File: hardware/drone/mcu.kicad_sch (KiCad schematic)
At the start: 18 parts, among them SW1 SW_MEC_5E, U1 STM32N645I0, U6 MX25UW25645GXDI00, Y3 Crystal_GND24

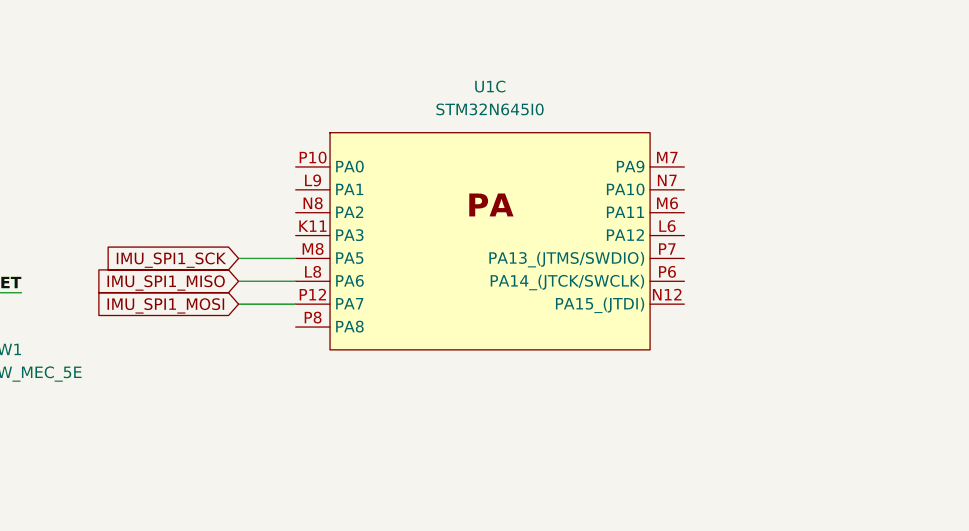
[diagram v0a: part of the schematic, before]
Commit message: Implemented power mux to select between battery and usb c 5V
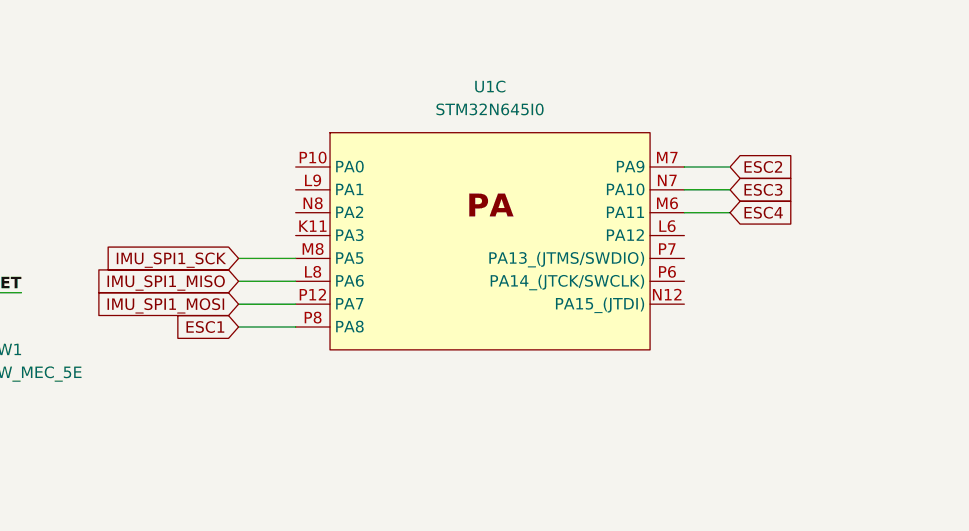
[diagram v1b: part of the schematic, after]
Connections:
- net ESC4: now reaches U1.M6 (PA11)
- net ESC2: now reaches U1.M7 (PA9)
- net ESC3: now reaches U1.N7 (PA10)
- net ESC1: now reaches U1.P8 (PA8)
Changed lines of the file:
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@@
+	(wire
+		(pts
+			(xy 179.07 48.26) (xy 173.99 48.26)
+		)
+		(stroke
+			(width 0)
+			(type default)
+		)
+	)
 	(wire
 		(pts
@@
 	(wire
 		(pts
+			(xy 124.46 60.96) (xy 130.81 60.96)
+		)
+		(stroke
+			(width 0)
+			(type default)
+		)
+	)
+	(wire
+		(pts
 			(xy 82.55 208.28) (xy 102.87 208.28)
 		)
@@
 	(wire
 		(pts
+			(xy 179.07 43.18) (xy 173.99 43.18)
+		)
+		(stroke
+			(width 0)
+			(type default)
+		)
+	)
+	(wire
+		(pts
 			(xy 116.84 191.77) (xy 116.84 187.96)
 		)
@@
 		(pts
 			(xy 143.51 118.11) (xy 137.16 118.11)
+		)
+		(stroke
+			(width 0)
+			(type default)
+		)
+	)
+	(wire
+		(pts
+			(xy 179.07 45.72) (xy 173.99 45.72)
 		)
 		(stroke
@@
 		)
 	)
+	(global_label "ESC1"
+		(shape input)
+		(at 124.46 60.96 180)
+		(fields_autoplaced yes)
+		(effects
+			(font
+				(size 1.27 1.27)
+			)
+			(justify right)
+		)
+		(property "Intersheetrefs" "${INTERSHEET_REFS}"
+			(at 116.6368 60.96 0)
+			(hide yes)
+			(show_name no)
+			(do_not_autoplace no)
+			(effects
+				(font
+					(size 1.27 1.27)
+				)
+				(justify right)
+			)
+		)
+	)
 	(global_label "PWR_ON"
 		(shape input)
@@
 		)
 	)
+	(global_label "ESC2"
+		(shape input)
+		(at 179.07 43.18 0)
+		(fields_autoplaced yes)
+		(effects
+			(font
+				(size 1.27 1.27)
+			)
+			(justify left)
+		)
+		(property "Intersheetrefs" "${INTERSHEET_REFS}"
+			(at 186.8932 43.18 0)
+			(hide yes)
+			(show_name no)
+			(do_not_autoplace no)
+			(effects
+				(font
+					(size 1.27 1.27)
+				)
+				(justify left)
+			)
+		)
+	)
 	(global_label "GNSS_UART4_TX_1V8"
 		(shape input)
@@
 		)
 	)
+	(global_label "ESC3"
+		(shape input)
+		(at 179.07 45.72 0)
+		(fields_autoplaced yes)
+		(effects
+			(font
+				(size 1.27 1.27)
+			)
+			(justify left)
+		)
+		(property "Intersheetrefs" "${INTERSHEET_REFS}"
+			(at 186.8932 45.72 0)
+			(hide yes)
+			(show_name no)
+			(do_not_autoplace no)
+			(effects
+				(font
+					(size 1.27 1.27)
+				)
+				(justify left)
+			)
+		)
+	)
 	(global_label "CC_SDMMC1_D1"
 		(shape input)
@@
 			)
 		)
+	)
+	(global_label "ESC4"
+		(shape input)
+		(at 179.07 48.26 0)
+		(fields_autoplaced yes)
+		(effects
+			(font
+				(size 1.27 1.27)
+			)
+			(justify left)
+		)
+		(property "Intersheetrefs" "${INTERSHEET_REFS}"
+			(at 186.8932 48.26 0)
+			(hide yes)
+			(show_name no)
+			(do_not_autoplace no)
+			(effects
+				(font
+					(size 1.27 1.27)
+				)
+				(justify left)
+			)
+		)

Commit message: Added barometer, more pinmuxxing, added VBAT sensing and reverse voltage protection
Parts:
- added C92: 100n, symbol Device:C
- added R25, R26: 49.9k, BM08BSRSSTBLFSN, symbol Device:R
- added R27: 2.49k, BM08BSRSSTBLFSN, symbol Device:R
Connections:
- net GND: now also C92.2, R27.1
- net at U1.L6 (PA12): now also C92.1, R26.1, R27.2
- net CODEC_I2C2_SCL renamed I2C2_SCL
- net CODEC_I2C2_SDA renamed I2C2_SDA
- new net: R25.1, R26.2
- new net VBAT: R25.2
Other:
- moved on the sheet: R13, R14, U1D, U1F, U1G

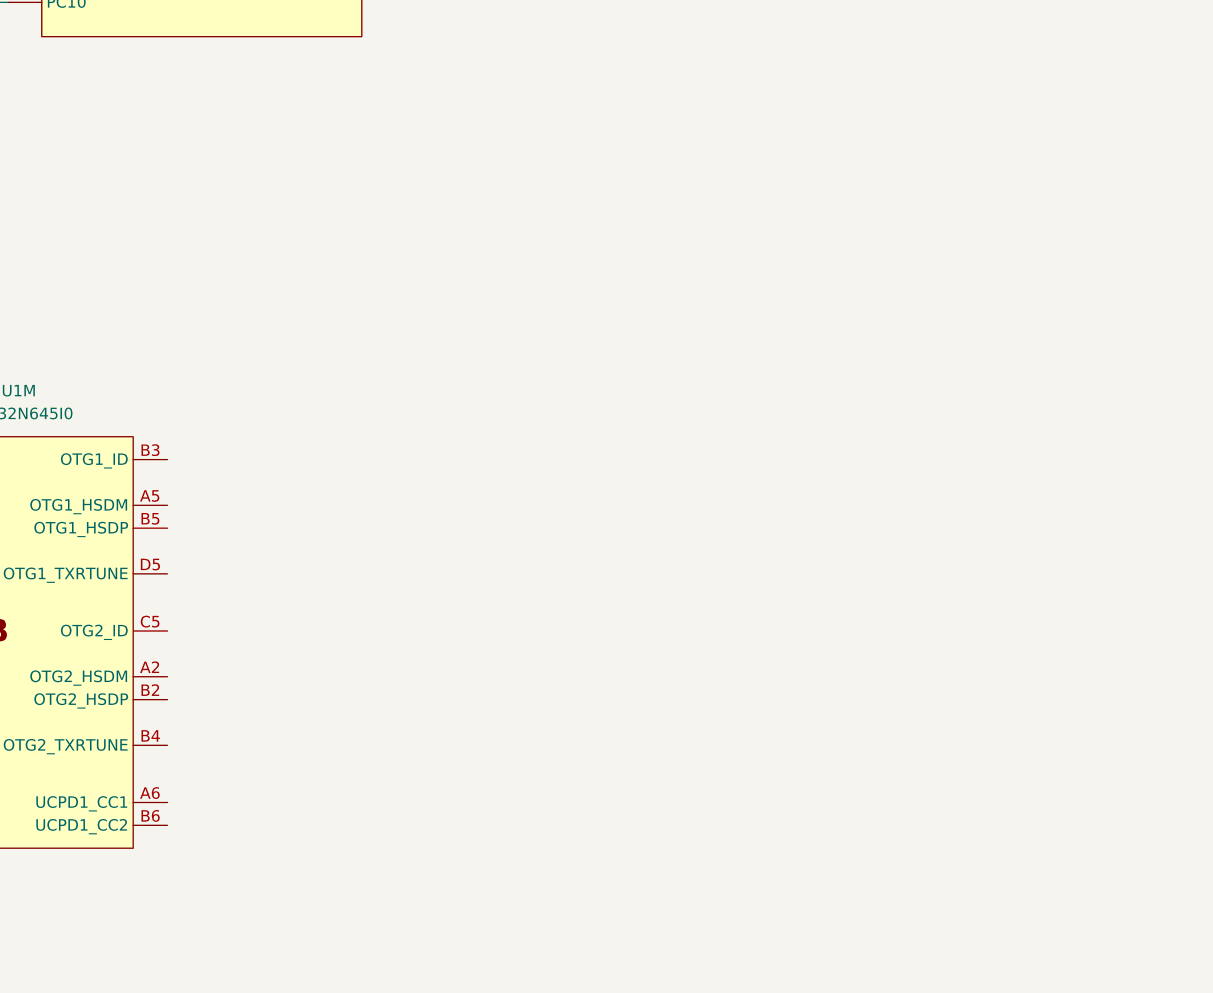
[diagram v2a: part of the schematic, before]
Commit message: Added USB C
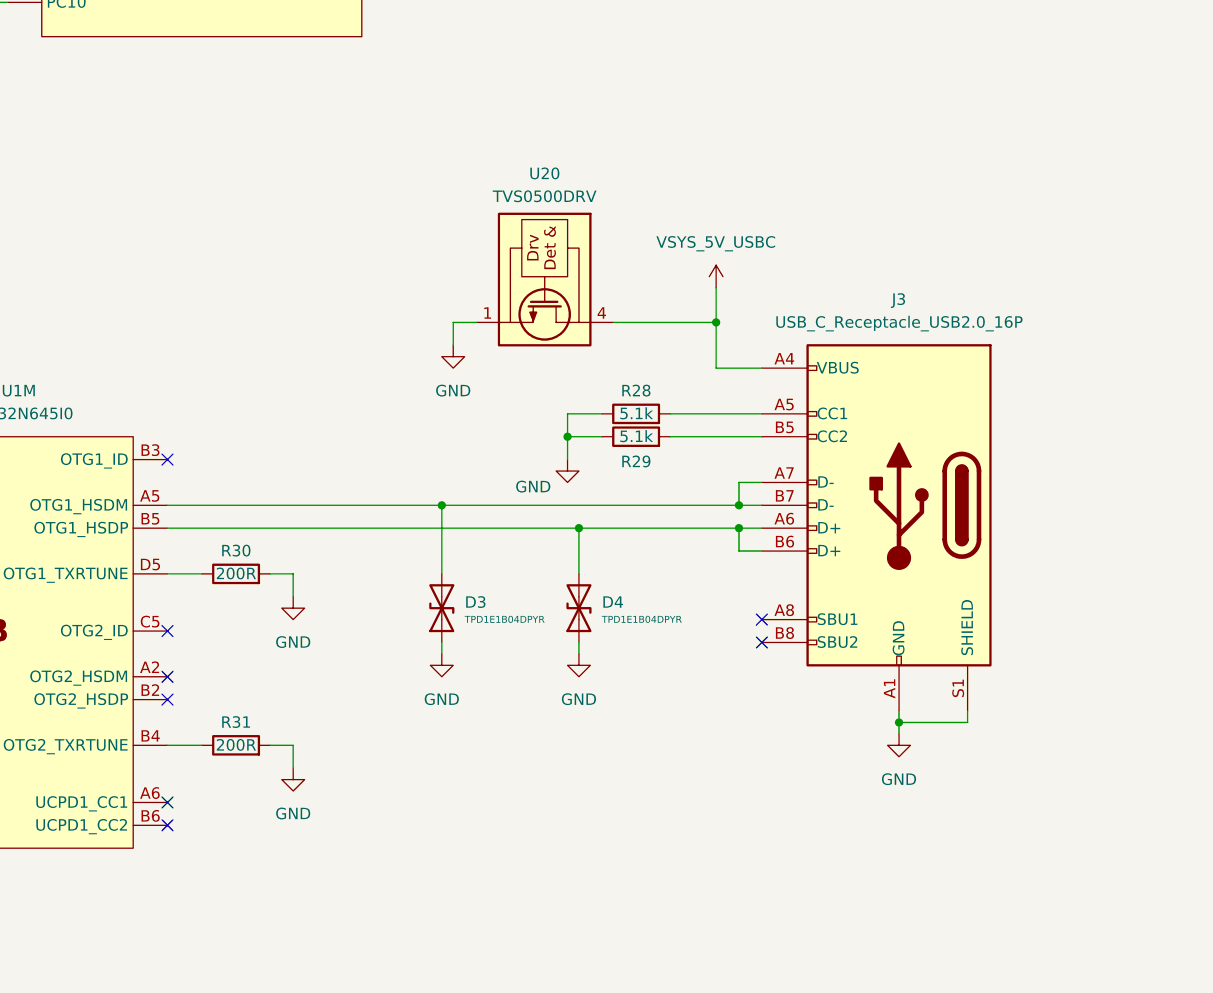
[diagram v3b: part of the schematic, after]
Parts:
- added D3, D4: TPD1E1B04DPYR, Package_DIP:DIP-40_W15.24mm, symbol Device:D_TVS
- added J3: USB_C_Receptacle_USB2.0_16P, symbol Connector:USB_C_Receptacle_USB2.0_16P
- added R28, R29: 5.1k, BM08BSRSSTBLFSN, symbol Device:R
- added R30, R31: 200R, symbol Device:R
- added U20: TVS0500DRV, Package_SON:WSON-6-1EP_2x2mm_P0.65mm_EP1x1.6mm, symbol Power_Protection:TVS0500DRV
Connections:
- net GND: now also D3.1 (A1), D4.1 (A1), J3.A1 (GND), J3.A12 (GND), J3.B1 (GND), J3.B12 (GND), J3.S1 (SHIELD), R28.1, R29.1, R30.2, R31.2, U20.1 (GND), U20.2 (GND), U20.3 (GND), U20.7 (GND)
- net at U1.A5 (OTG1_HSDM): now also D3.2 (A2), J3.A7 (D-), J3.B7 (D-)
- net at U1.B4 (OTG2_TXRTUNE): now also R31.1
- net at U1.B5 (OTG1_HSDP): now also D4.2 (A2), J3.A6 (D+), J3.B6 (D+)
- net at U1.D5 (OTG1_TXRTUNE): now also R30.1
- new net: J3.A5 (CC1), R28.2
- new net: J3.B5 (CC2), R29.2
- new net VSYS_5V_USBC: J3.A4 (VBUS), J3.A9 (VBUS), J3.B4 (VBUS), J3.B9 (VBUS), U20.4 (IN), U20.5 (IN), U20.6 (IN)
- no-connect marks 0 -> 8

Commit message: Added SWD
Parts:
- added C93: 10u, symbol Device:C
- added C94: 100n, symbol Device:C
- added J4: Conn_ARM_SWD_TagConnect_TC2030, Connector:Tag-Connect_TC2030-IDC-FP_2x03_P1.27mm_Vertical, symbol Connector:Conn_ARM_SWD_TagConnect_TC2030
- C1: value C -> 10n
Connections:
- net GND: now also C93.2, C94.2, J4.5 (GND)
- net VDD1V8: now also J4.1 (VCC)
- net VSYS_5V_USBC: now also C93.1, C94.1
- net SWO: now reaches U1.M11 (PB5_(JTDO/TRACESWO))
- net SWO: now also J4.6 (SWO)
- net SWCLK: now reaches U1.P6 (PA14_(JTCK/SWCLK))
- net SWCLK: now also J4.4 (SWCLK)
- net SWDIO: now reaches U1.P7 (PA13_(JTMS/SWDIO))
- net SWDIO: now also J4.2 (SWDIO)
- net RESET renamed NRST
- net NRST: now also J4.3 (~{RESET})
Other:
- note added: "USB C"
- moved on the sheet: C29, C30, C31, C32, C33, C34, D3, D4, J3, R28, R29, R30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

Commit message: Finished MCU schematic decoupling, finished system control schematic
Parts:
- added R32: 10k, symbol Device:R
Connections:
- net GND: now also R32.2
- net VDDA1V8: now also U1.A1 (PDR_ON)
- net at U1.D3 (BOOT0): now also R32.1
- net I2C1_SDA: now reaches U1.B8 (PC1)
- net IMU_CS: now reaches U1.G14 (PB0)
- net IMU_SPI4_MOSI: now reaches U1.H13 (PB7)
- net IMU_SPI4_MISO: now reaches U1.H14 (PB6)
- net IMU_SPI4_SCK: now reaches U1.F14 (PE2)
- net I2C1_SCL: now reaches U1.C8 (PH9)
- net IMU_SPI1_MISO: no longer names the net of U1.L8 (PA6)
- net IMU_SPI1_MOSI: no longer names the net of U1.P12 (PA7)
- net IMU_SPI1_SCK: no longer names the net of U1.M8 (PA5)
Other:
- moved on the sheet: R13, R14, U1G

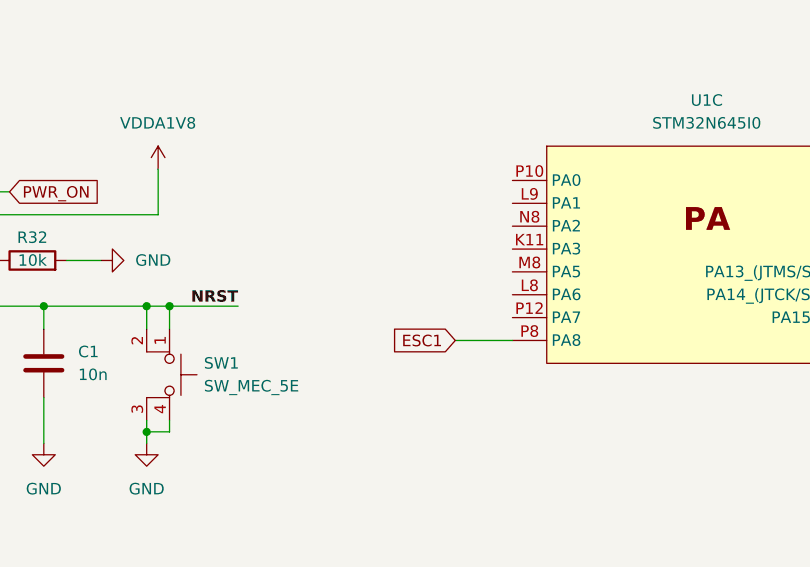
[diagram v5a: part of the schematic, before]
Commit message: Fixed BOOT1 pulldown
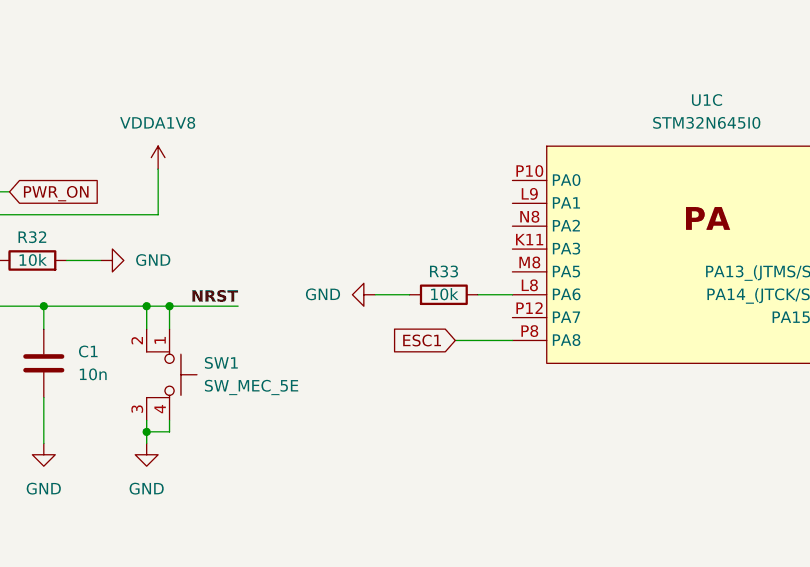
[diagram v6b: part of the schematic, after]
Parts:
- added R33: 10k, symbol Device:R
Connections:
- net GND: now also R33.2
- net at U1.L8 (PA6): now also R33.1
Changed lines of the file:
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@@
+	(wire
+		(pts
+			(xy 130.81 55.88) (xy 127 55.88)
+		)
+		(stroke
+			(width 0)
+			(type default)
+		)
+	)
 	(wire
 		(pts
@@
 		(pts
 			(xy 125.73 170.18) (xy 125.73 171.45)
+		)
+		(stroke
+			(width 0)
+			(type default)
+		)
+	)
+	(wire
+		(pts
+			(xy 119.38 55.88) (xy 115.57 55.88)
 		)
 		(stroke
@@
 					(unit 1)
 				)
+			)
+		)
+	)
+	(symbol
+		(lib_id "Device:R")
+		(at 123.19 55.88 270)
+		(mirror x)
+		(unit 1)
+		(body_style 1)
+		(exclude_from_sim no)
+		(in_bom yes)
+		(on_board yes)
+		(in_pos_files yes)
+		(dnp no)
+		(property "Reference" "R33"
+			(at 123.19 53.34 90)
+			(show_name no)
+			(do_not_autoplace no)
+			(effects
+				(font
+					(size 1.27 1.27)
+				)
+			)
+		)
+		(property "Value" "10k"
+			(at 123.19 55.88 90)
+			(show_name no)
+			(do_not_autoplace no)
+			(effects
+				(font
+					(size 1.27 1.27)
+				)
+			)
+		)
+		(property "Footprint" ""
+			(at 123.19 57.658 90)
+			(hide yes)
+			(show_name no)
+			(do_not_autoplace no)
+			(effects
+				(font
+					(size 1.27 1.27)
+				)
+			)
+		)
+		(property "Datasheet" ""
+			(at 123.19 55.88 0)
+			(hide yes)
+			(show_name no)
+			(do_not_autoplace no)
+			(effects
+				(font
+					(size 1.27 1.27)
+				)
+			)
+		)
+		(property "Description" "Resistor"
+			(at 123.19 55.88 0)
+			(hide yes)
+			(show_name no)
+			(do_not_autoplace no)
+			(effects
+				(font
+					(size 1.27 1.27)
+				)
+			)
+		)
+		(pin "1"
+		)
+		(pin "2"
+		)
+		(instances
+			(project "drone"
+				(path "/62c402a6-ed3f-446b-8423-821e9cc6908b/93cf7a35-4ece-42f4-8b64-ee97cf1aaf17"
+					(reference "R33")
+					(unit 1)
+				)
+			)
+		)
+	)
+	(symbol
+		(lib_id "power:GND")
+		(at 115.57 55.88 270)
+		(mirror x)
+		(unit 1)
+		(body_style 1)
+		(exclude_from_sim no)
+		(in_bom yes)
+		(on_board yes)
+		(in_pos_files yes)
+		(dnp no)
+		(fields_autoplaced yes)
+		(property "Reference" "#PWR0184"
+			(at 109.22 55.88 0)
+			(hide yes)
+			(show_name no)
+			(do_not_autoplace no)
+			(effects
+				(font
+					(size 1.27 1.27)
+				)
+			)
+		)
+		(property "Value" "GND"
+			(at 111.76 55.8799 90)
+			(show_name no)
+			(do_not_autoplace no)
+			(effects
+				(font
+					(size 1.27 1.27)
+				)
+				(justify right)
+			)
+		)
+		(property "Footprint" ""
+			(at 115.57 55.88 0)
+			(hide yes)
+			(show_name no)
+			(do_not_autoplace no)
+			(effects
+				(font
+					(size 1.27 1.27)
+				)
+			)
+		)
+		(property "Datasheet" ""
+			(at 115.57 55.88 0)
+			(hide yes)
+			(show_name no)
+			(do_not_autoplace no)
+			(effects
+				(font
+					(size 1.27 1.27)
+				)
+			)
+		)
+		(property "Description" "Power symbol creates a global label with name \"GND\" , ground"
+			(at 115.57 55.88 0)
+			(hide yes)
+			(show_name no)
+			(do_not_autoplace no)
+			(effects
+				(font
+					(size 1.27 1.27)
+				)
+			)
+		)
+		(pin "1"
+		)
+		(instances
+			(project "drone"
+				(path "/62c402a6-ed3f-446b-8423-821e9cc6908b/93cf7a35-4ece-42f4-8b64-ee97cf1aaf17"
+					(reference "#PWR0184")
+					(unit 1)
+				)

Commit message: Created pinmux table and completed pinmuxing
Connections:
- net CODEC_SAI2_SD_B: no longer U1.J4 (PF5)
- net GNSS_RESET_N_1V8: now reaches U1.A13 (PD3)
- net EN_MODULE: now reaches U1.B11 (PD7)
- net GNSS_TIMEPULSE: now reaches U1.E10 (PD2)
- net CC_IRQ_WL: now reaches U1.A8 (PC6)
- net CC_RESET: now reaches U1.A9 (PC7)
- net IMU_INT1: now reaches U1.M10 (PB12)
- net NRST_CAM: now reaches U1.B10 (PE15)
- net CODEC_IRQ: now reaches U1.C9 (PE14)
- net BARO_IRQ: now reaches U1.L12 (PG8)
- net SX_IRQ: now reaches U1.J3 (PF10)
- net SX_NRST: now reaches U1.L1 (PF8)
- net SX_BUSY: now reaches U1.L2 (PF11)
- new net CODEC_SAI2_SD_A: U1.J4 (PF5)
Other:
- moved on the sheet: J4

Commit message: Added magnetometer
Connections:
- net MAG_INT: now reaches U1.L9 (PA1)
